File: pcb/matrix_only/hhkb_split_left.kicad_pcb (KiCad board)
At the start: 2 copper layers, 138.4 x 97.4 mm, 65 parts, among them SW1 CPG151101S11-2, SW10 CPG151101S11-2, SW11 CPG151101S11-2, SW12 CPG151101S11-2, SW13 CPG151101S11-2, SW14 CPG151101S11-2, SW15 CPG151101S11-2, SW16 CPG151101S11-2, SW17 CPG151101S11-2, SW18 CPG151101S11-2, SW19 CPG151101S11-2, SW2 CPG151101S11-2, SW20 CPG151101S11-2, SW21 CPG151101S11-2, SW22 CPG151101S11-2, SW23 CPG151101S11-2, SW24 CPG151101S11-2, SW25 CPG151101S11-2, SW26 CPG151101S11-2, SW27 CPG151101S11-2, SW3 CPG151101S11-2, SW4 CPG151101S11-2, SW5 CPG151101S11-2, SW6 CPG151101S11-2, SW7 CPG151101S11-2, SW8 CPG151101S11-2, SW9 CPG151101S11-2, U1 74LVC595

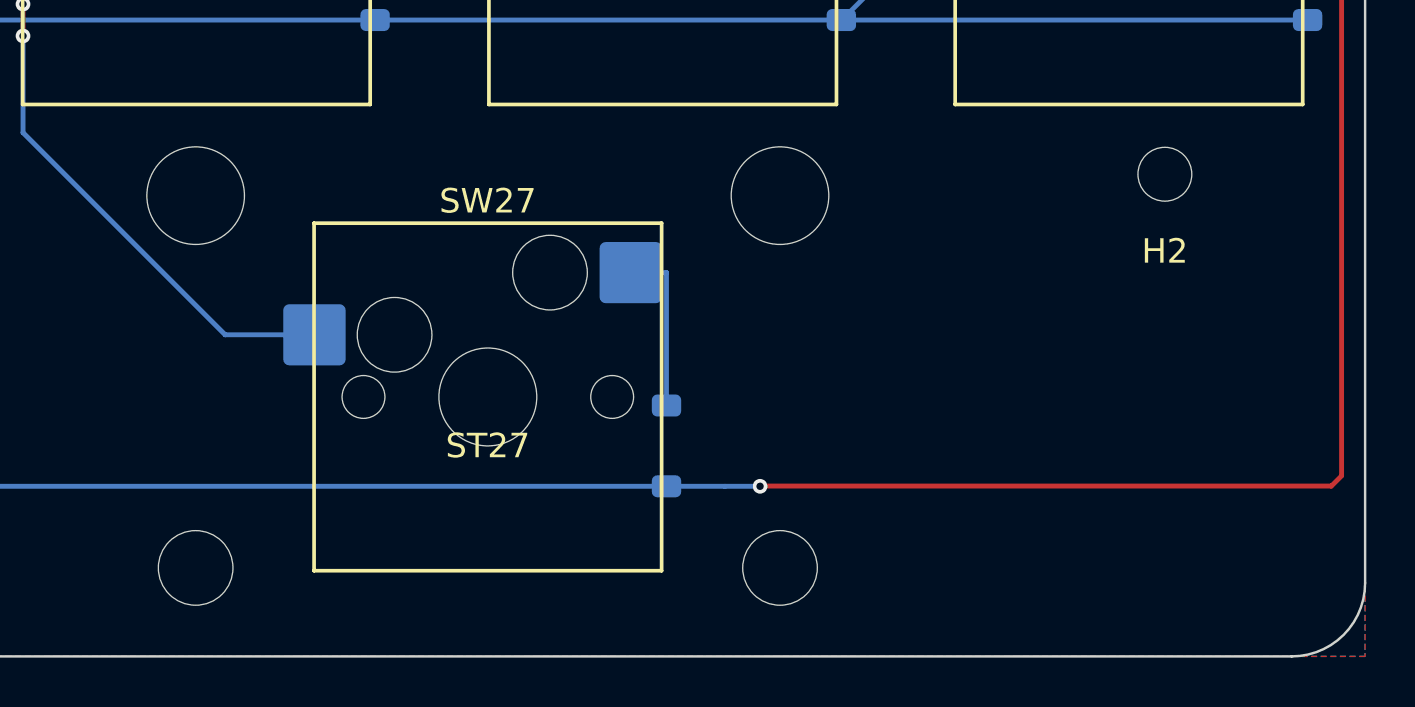
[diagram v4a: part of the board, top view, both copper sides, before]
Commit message: open-gaps #56: スペースを両島の内側端へ寄せ直し（左 4.5〜7.25u・右 9.75〜12.5u、Meta との空き左右対称 0.5u）
- layout: 最下段のみ。Alt 1u / Meta 1.5u は原機の位置のまま（利用者確認）
- 基板の柱 左 H2 (64,−30)・右 H4 (−81,−38)。柱がキーの真下に立つ取り違えを
  test_pcb_posts_do_not_touch_any_key で見る（H4 を戻すと落ちる）
- matrix_only: SW27/ST27/D27・SW32/ST32/D32 を API で移動し配線を引き直し。
  キー名シルクは部品に付いてこないので手で移動（handover の「落ちる穴」に追記）
- export_matrix_routing → gen_pcb → finalize_pcb → pcb_parts → drc。
  3 基板 DRC 0 / 未配線 0、警告は元の 37 / 41 / 1。スタビ同心 0.000・180°・縁 2.14mm
- #21: DSA 1u/1.5u/1.75u/2.25u/2.75u が SP 直販で単品・在庫ありと確認。
  2.75u の外側マウント 0.469"＝11.9mm は Cherry 2u スタビと一致
- pytest 479 passed

Co-Authored-By: Claude Fable 5 <noreply@anthropic.com>
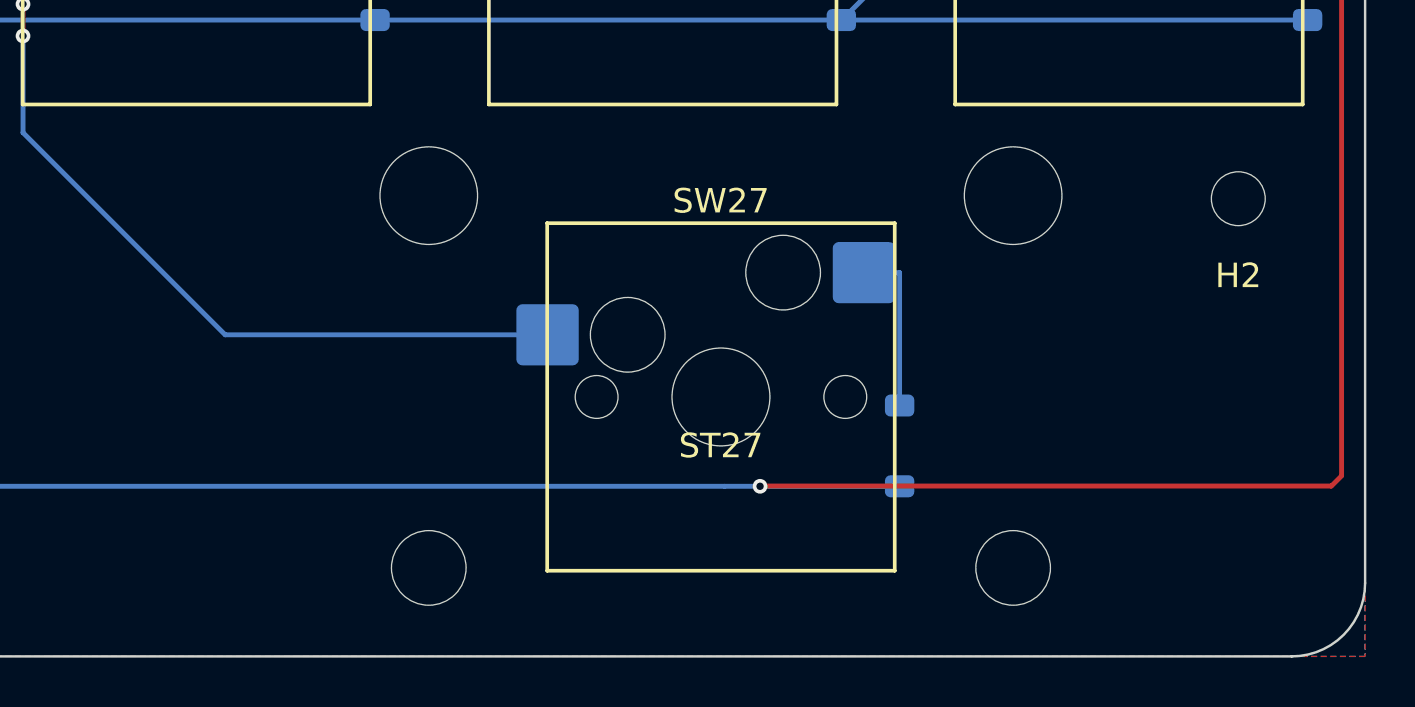
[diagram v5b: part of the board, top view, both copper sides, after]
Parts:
- moved D27 9.53 mm to (200.2, 140.1)
- moved ST27 9.53 mm to (192.9, 138.1)
- moved SW27 9.53 mm to (192.9, 138.1)
- moved H2 3.16 mm to (214.0, 130.0)
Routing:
- net COL3: track 135.3 -> 144.9 mm
- net ROW_A: track 161.7 -> 167.4 mm
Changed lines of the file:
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@@
 	(footprint "SW_Hotswap_Kailh_MX_2.75u"
 		(layer "F.Cu")
-		(at 183.3375 138.1)
+		(at 192.8625 138.1)
 		(descr "Kailh keyswitch Hotswap Socket Keycap 2.75u")
 		(tags "Kailh Keyboard Keyswitch Switch Hotswap Socket Relief Cutout Keycap 2.75u")
@@
 	(footprint "Stabilizer_Cherry_MX_2.00u"
 		(layer "F.Cu")
-		(at 183.3375 138.1 180)
+		(at 192.8625 138.1 180)
 		(descr "Cherry MX PCB Stabilizer 2.00u 2.25u 2.50u 2.75u")
 		(tags "Cherry MX Keyboard Stabilizer 2.00u 2.25u 2.50u 2.75u Cutout")
@@
 	(footprint "MountingHole_2.2mm_M2"
 		(layer "F.Cu")
-		(at 211 129)
+		(at 214 130)
 		(descr "Mounting Hole 2.2mm, M2, no annular, generated by kicad-footprint-generator mountinghole.py")
 		(tags "mountinghole M2")
@@
 	(footprint "D_SOD-123"
 		(layer "B.Cu")
-		(at 190.6375 140.1 90)
+		(at 200.1625 140.1 90)
 		(descr "SOD-123")
 		(tags "SOD-123")
@@
 		)
 	)
-	(gr_text "L-Space"
-		(at 185.71875 129.9 0)
+	(gr_text "V"
+		(at 190.48125 110.85 0)
 		(layer "B.SilkS")
 		(effects
@@
 		)
 	)
-	(gr_text "V"
-		(at 190.48125 110.85 0)
+	(gr_text "L-Space"
+		(at 192.8625 129.9 0)
 		(layer "B.SilkS")
 		(effects
@@
 	)
 	(segment
-		(start 172.606 135.56)
-		(end 176.2525 135.56)
-		(width 0.2)
-		(layer "B.Cu")
-		(net "COL3")
-	)
-	(segment
 		(start 154.8212 104.3)
 		(end 154.8212 106.985)
@@
 	)
 	(segment
+		(start 172.61 135.56)
+		(end 185.78 135.56)
+		(width 0.2)
+		(layer "B.Cu")
+		(net "COL3")
+	)
+	(segment
 		(start 140.5337 68.885)
 		(end 150.0588 78.41)
@@
 	)
 	(segment
-		(start 190.63755 133.02)
-		(end 190.63755 138.45)
+		(start 198.7 133.02)
+		(end 200.16 133.02)
 		(width 0.2)
 		(layer "B.Cu")
@@
 	)
 	(segment
-		(start 189.17955 133.02)
-		(end 190.63755 133.02)
+		(start 200.16 133.02)
+		(end 200.16 138.45)
 		(width 0.2)
 		(layer "B.Cu")
@@
 		(width 0.2)
 		(layer "B.Cu")
+		(net "ROW_A")
+	)
+	(segment
+		(start 194.46 141.75)
+		(end 200.16 141.75)
+		(width 0.2)
+		(layer "B.Cu")
